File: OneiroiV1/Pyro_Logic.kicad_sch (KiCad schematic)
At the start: 40 parts, among them J17 TB002-500-02BE, J18 TB002-500-02BE, J19 TB002-500-02BE, J20 TB002-500-02BE, J21 TB002-500-02BE, J22 TB002-500-02BE, Q1 SI4909DY-T1-GE3, Q2 MBT3904DW1T1G, U4 DMP3085LSD-13, U7 MMDT5551-7-F

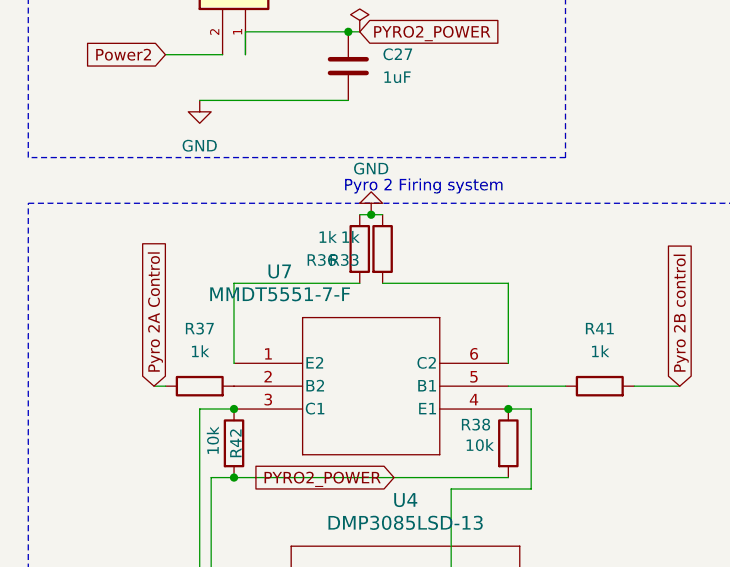
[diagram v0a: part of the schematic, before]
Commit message: Oneiroi Changes
All 3D models and footprints updated to common library, silkscreening must be re-done.
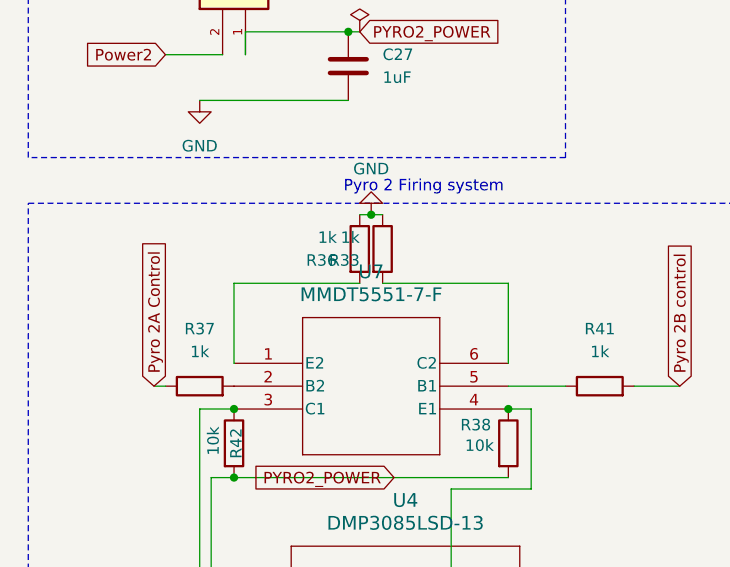
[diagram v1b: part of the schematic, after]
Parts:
- J17, J18, J19, J20, J21, J22: footprint screw terminal:CUI_TB002-500-02BE -> UNSW Rocketry Library:CUI_TB002-500-02BE; symbol screw terminal:TB002-500-02BE -> UNSW Rocketry Library:TB002-500-02BE
- Q1: footprint pyro 1:SOIC_09DY-T1-GE3_VIS -> UNSW Rocketry Library:SOIC_09DY-T1-GE3_VIS; symbol PMOS MOSFET 1:SI4909DY-T1-GE3 -> UNSW Rocketry Library:SI4909DY-T1-GE3
- Q2: footprint npn 1:SOT-363&slash_SC-88&slash_SC70-6&slash_CASE419B_OSI -> UNSW Rocketry Library:SOT-363&slash_SC-88&slash_SC70-6&slash_CASE419B_OSI; symbol NPN BJT 1:MBT3904DW1T1G -> UNSW Rocketry Library:MBT3904DW1T1G
- U4: footprint pyro 2:IC_DMP3028LSD-13_DIO -> UNSW Rocketry Library:IC_DMP3028LSD-13_DIO; symbol PMOS MOSFET 2:DMP3085LSD-13 -> UNSW Rocketry Library:DMP3085LSD-13
- U7: footprint npn 2:SOT-363_DIO -> UNSW Rocketry Library:SOT-363_DIO; symbol NPN BJT 2:MMDT5551-7-F -> UNSW Rocketry Library:MMDT5551-7-F
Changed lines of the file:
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@@
 	)
 	(symbol
-		(lib_id "screw terminal:TB002-500-02BE")
+		(lib_id "UNSW Rocketry Library:TB002-500-02BE")
 		(at 39.37 21.59 270)
 		(mirror x)
@@
 			)
 		)
-		(property "Footprint" "screw terminal:CUI_TB002-500-02BE"
+		(property "Footprint" "UNSW Rocketry Library:CUI_TB002-500-02BE"
 			(at 39.37 21.59 0)
 			(hide yes)
@@
 	)
 	(symbol
-		(lib_id "screw terminal:TB002-500-02BE")
+		(lib_id "UNSW Rocketry Library:TB002-500-02BE")
 		(at 55.88 128.27 0)
 		(unit 1)
@@
 			)
 		)
-		(property "Footprint" "screw terminal:CUI_TB002-500-02BE"
+		(property "Footprint" "UNSW Rocketry Library:CUI_TB002-500-02BE"
 			(at 55.88 128.27 0)
 			(hide yes)
@@
 	)
 	(symbol
-		(lib_id "PMOS MOSFET 1:SI4909DY-T1-GE3")
+		(lib_id "UNSW Rocketry Library:SI4909DY-T1-GE3")
 		(at 217.17 95.25 0)
 		(unit 1)
@@
 			)
 		)
-		(property "Footprint" "pyro 1:SOIC_09DY-T1-GE3_VIS"
+		(property "Footprint" "UNSW Rocketry Library:SOIC_09DY-T1-GE3_VIS"
 			(at 217.17 95.25 0)
 			(hide yes)
@@
 	)
 	(symbol
-		(lib_id "NPN BJT 2:MMDT5551-7-F")
+		(lib_id "UNSW Rocketry Library:MMDT5551-7-F")
 		(at 20.32 66.04 0)
 		(unit 1)
@@
 		(fields_autoplaced yes)
 		(property "Reference" "U7"
-			(at 45.72 55.88 0)
+			(at 55.88 55.88 0)
 			(show_name no)
 			(do_not_autoplace no)
@@
 		)
 		(property "Value" "MMDT5551-7-F"
-			(at 45.72 58.42 0)
+			(at 55.88 58.42 0)
 			(show_name no)
 			(do_not_autoplace no)
@@
 			)
 		)
-		(property "Footprint" "npn 2:SOT-363_DIO"
-			(at 20.32 66.04 0)
+		(property "Footprint" "UNSW Rocketry Library:SOT-363_DIO"
+			(at 40.64 66.04 0)
 			(hide yes)
 			(show_name no)
@@
 		)
 		(property "Datasheet" "MMDT5551-7-F"
-			(at 20.32 66.04 0)
+			(at 40.64 66.04 0)
 			(hide yes)
 			(show_name no)
@@
 	)
 	(symbol
-		(lib_id "NPN BJT 1:MBT3904DW1T1G")
+		(lib_id "UNSW Rocketry Library:MBT3904DW1T1G")
 		(at 215.9 72.39 0)
 		(unit 1)
@@
 			)
 		)
-		(property "Footprint" "npn 1:SOT-363&slash_SC-88&slash_SC70-6&slash_CASE419B_OSI"
+		(property "Footprint" "UNSW Rocketry Library:SOT-363&slash_SC-88&slash_SC70-6&slash_CASE419B_OSI"
 			(at 215.9 72.39 0)
 			(hide yes)
@@
 	)
 	(symbol
-		(lib_id "screw terminal:TB002-500-02BE")
+		(lib_id "UNSW Rocketry Library:TB002-500-02BE")
 		(at 238.76 17.78 90)
 		(unit 1)
@@
 			)
 		)
-		(property "Footprint" "screw terminal:CUI_TB002-500-02BE"
+		(property "Footprint" "UNSW Rocketry Library:CUI_TB002-500-02BE"
 			(at 238.76 17.78 0)
 			(hide yes)
@@
 	)
 	(symbol
-		(lib_id "screw terminal:TB002-500-02BE")
+		(lib_id "UNSW Rocketry Library:TB002-500-02BE")
 		(at 241.3 148.59 0)
 		(mirror x)
@@
 			)
 		)
-		(property "Footprint" "screw terminal:CUI_TB002-500-02BE"
+		(property "Footprint" "UNSW Rocketry Library:CUI_TB002-500-02BE"
 			(at 241.3 148.59 0)
 			(hide yes)
@@
 	)
 	(symbol
-		(lib_id "PMOS MOSFET 2:DMP3085LSD-13")
+		(lib_id "UNSW Rocketry Library:DMP3085LSD-13")
 		(at 39.37 91.44 0)
 		(unit 1)
@@
 			)
 		)
-		(property "Footprint" "pyro 2:IC_DMP3028LSD-13_DIO"
+		(property "Footprint" "UNSW Rocketry Library:IC_DMP3028LSD-13_DIO"
 			(at 39.37 91.44 0)
 			(hide yes)
@@
 	)
 	(symbol
-		(lib_id "screw terminal:TB002-500-02BE")
+		(lib_id "UNSW Rocketry Library:TB002-500-02BE")
 		(at 55.88 120.65 0)
 		(unit 1)
@@
 			)
 		)
-		(property "Footprint" "screw terminal:CUI_TB002-500-02BE"
+		(property "Footprint" "UNSW Rocketry Library:CUI_TB002-500-02BE"
 			(at 55.88 120.65 0)
 			(hide yes)
@@
 	)
 	(symbol
-		(lib_id "screw terminal:TB002-500-02BE")
+		(lib_id "UNSW Rocketry Library:TB002-500-02BE")
 		(at 241.3 156.21 0)
 		(mirror x)
@@
 			)
 		)
-		(property "Footprint" "screw terminal:CUI_TB002-500-02BE"
+		(property "Footprint" "UNSW Rocketry Library:CUI_TB002-500-02BE"
 			(at 241.3 156.21 0)
 			(hide yes)
